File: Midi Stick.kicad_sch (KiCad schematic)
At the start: 34 parts, among them J1 USB 2.0 Type A Plug, J2 Aux, J3 ICSP, Q1 Mosfet N, X1 X1E0000210019

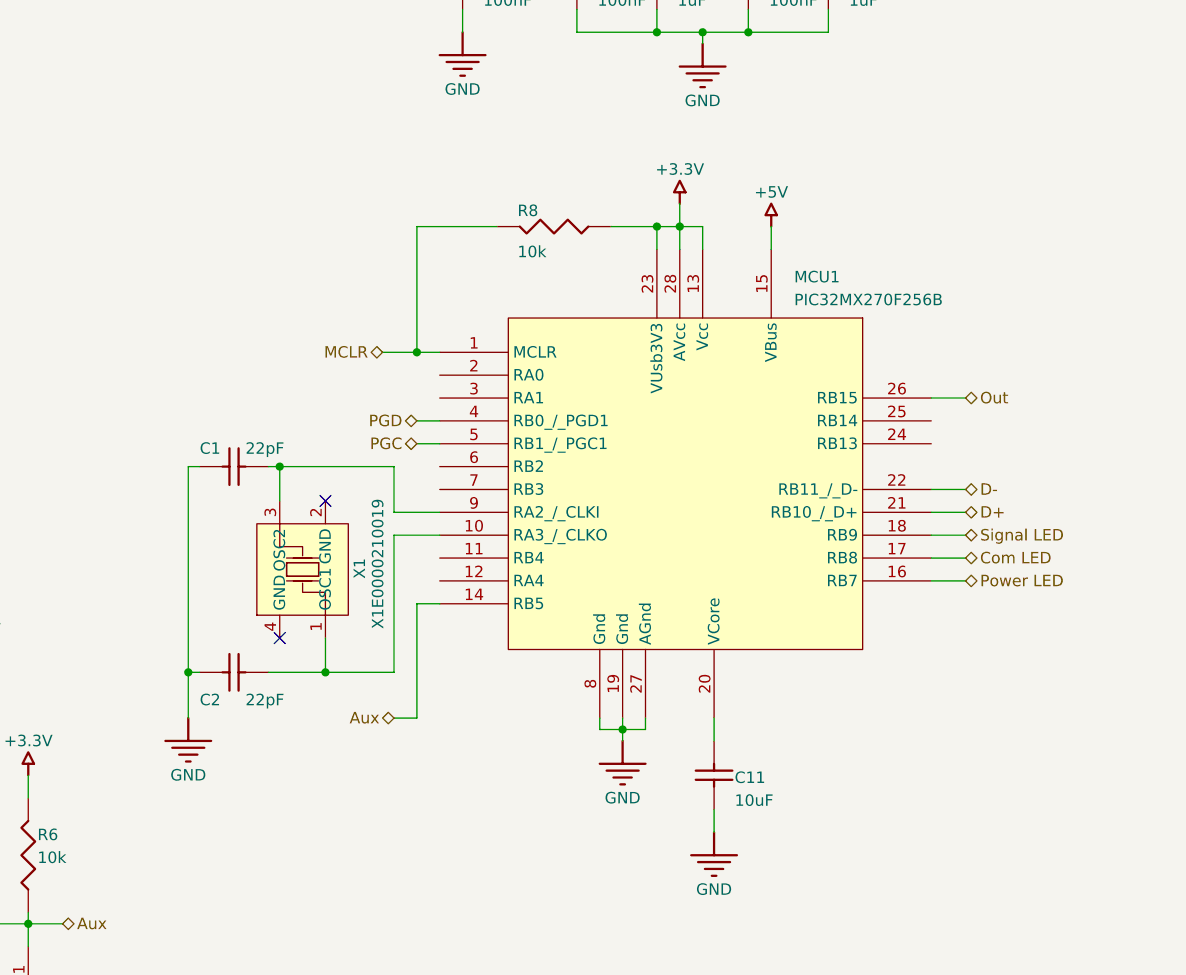
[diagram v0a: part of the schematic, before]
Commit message: Fix recommended minimum PIC32 connection
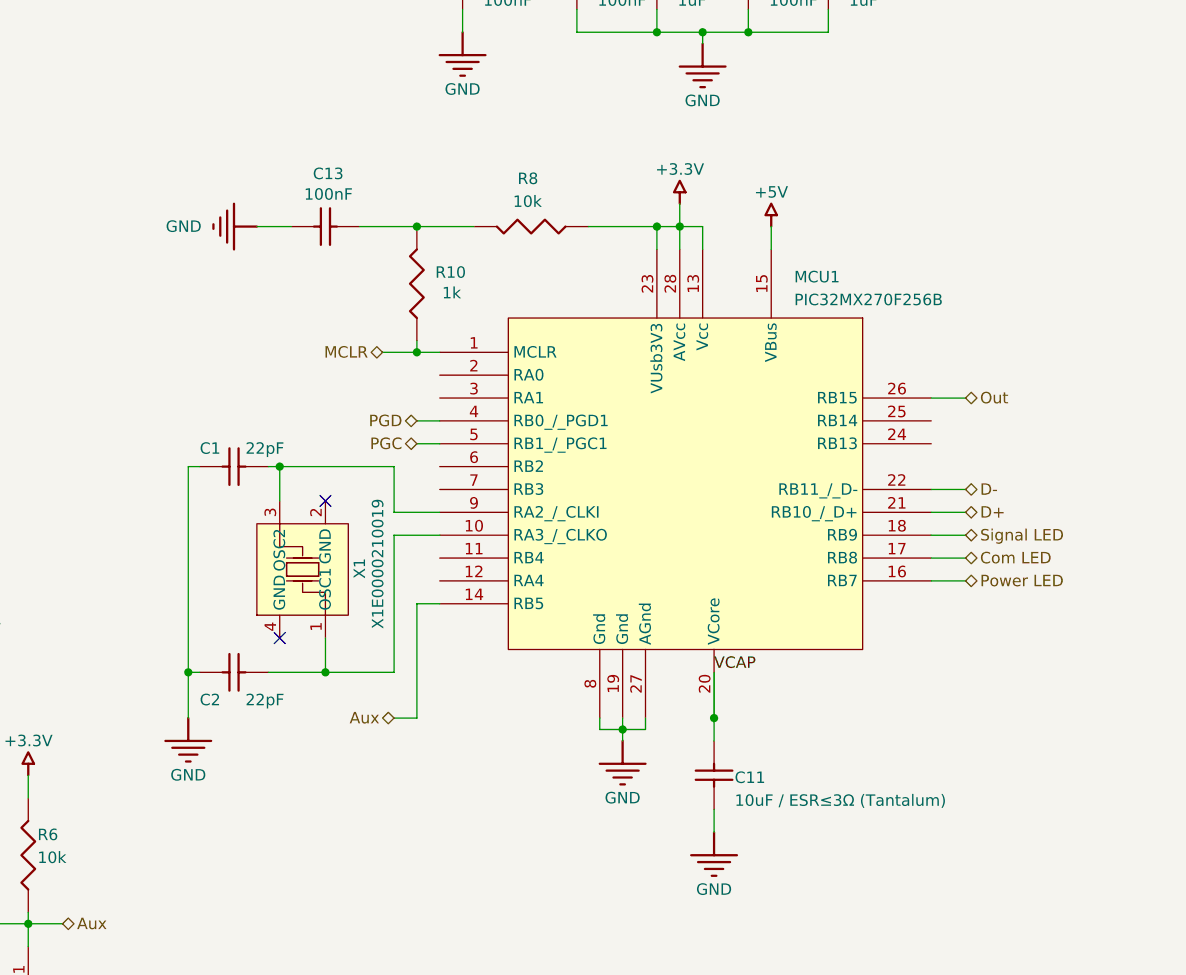
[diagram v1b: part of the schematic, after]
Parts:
- added C13: 100nF, Capacitor_SMD:C_0603_1608Metric, symbol Midi Stick-altium-import:root_1_Cap
- added R10: 1k, Resistor_SMD:R_0603_1608Metric, symbol Midi Stick-altium-import:root_1_Resistor
- C11: value 10uF -> 10uF / ESR≤3Ω (Tantalum); footprint Capacitor_SMD:C_0603_1608Metric -> Capacitor_SMD:C_1206_3216Metric
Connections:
- net GND: now also C13.2
- net MCLR: now also R10.1; no longer R8.2
- net VCAP: now reaches C11.2, MCU1.20 (VCore)
- new net: C13.1, R10.2, R8.2
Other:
- moved on the sheet: R8
